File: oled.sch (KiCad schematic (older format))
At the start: 3 parts

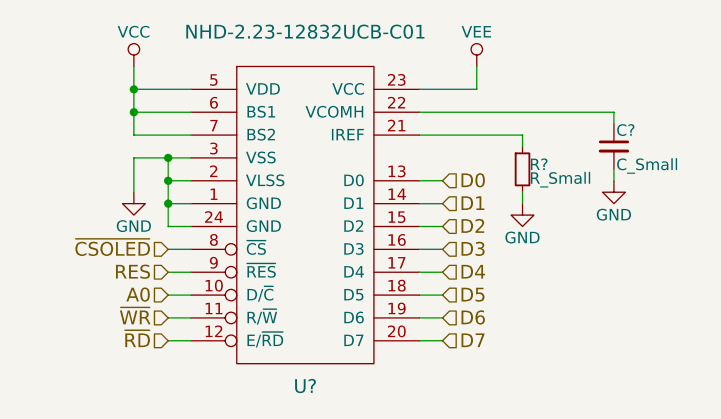
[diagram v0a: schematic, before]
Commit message: add more circuitry to schematic
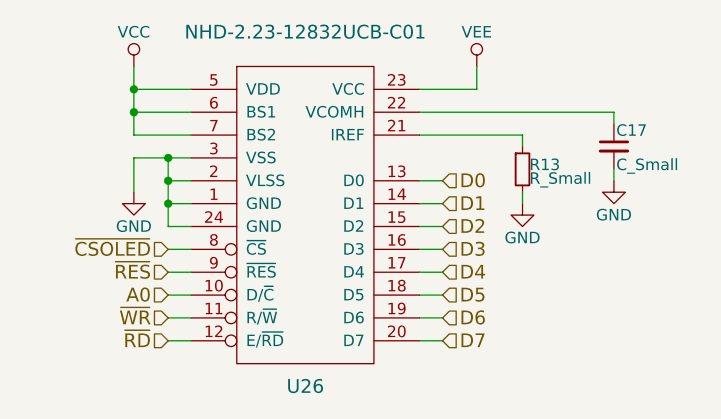
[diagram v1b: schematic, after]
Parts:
- gave numbers to parts that had none: 3
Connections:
- net RES renamed ~RES
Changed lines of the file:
@@
 $EndDescr
 $Comp
-L NHD-2.23-12832UCB-C01 U?
+L NHD-2.23-12832UCB-C01 U26
 U 1 1 576ACF58
 P 5500 3750
-F 0 "U?" H 5500 3000 60  0000 C CNN
+F 0 "U26" H 5500 3000 60  0000 C CNN
 F 1 "NHD-2.23-12832UCB-C01" H 5500 4550 60  0000 C CNN
 F 2 "" H 5500 3750 60  0000 C CNN
@@
 $EndComp
 $Comp
-L VCC #PWR?
+L VCC #PWR26
 U 1 1 576ACFE9
 P 4750 3100
-F 0 "#PWR?" H 4750 2950 50  0001 C CNN
+F 0 "#PWR26" H 4750 2950 50  0001 C CNN
 F 1 "VCC" H 4750 3250 50  0000 C CNN
 F 2 "" H 4750 3100 50  0000 C CNN
@@
 Connection ~ 4750 3300
 $Comp
-L GND #PWR?
+L GND #PWR29
 U 1 1 576AD010
 P 4750 3650
-F 0 "#PWR?" H 4750 3400 50  0001 C CNN
+F 0 "#PWR29" H 4750 3400 50  0001 C CNN
 F 1 "GND" H 4750 3500 50  0000 C CNN
 F 2 "" H 4750 3650 50  0000 C CNN
@@
 Text HLabel 4900 3900 0    60   Input ~ 0
 ~CSOLED
-Text HLabel 4900 4000 0    60   Input ~ 0
-RES
 Text HLabel 4900 4100 0    60   Input ~ 0
 A0
@@
 	6100 4300 6000 4300
 $Comp
-L VEE #PWR?
+L VEE #PWR27
 U 1 1 576CD337
 P 6250 3100
-F 0 "#PWR?" H 6250 2950 50  0001 C CNN
+F 0 "#PWR27" H 6250 2950 50  0001 C CNN
 F 1 "VEE" H 6250 3250 50  0000 C CNN
 F 2 "" H 6250 3100 50  0000 C CNN
@@
 	6250 3200 6250 3100
 $Comp
-L C_Small C?
+L C_Small C17
 U 1 1 576CD377
 P 6850 3450
-F 0 "C?" H 6860 3520 50  0000 L CNN
+F 0 "C17" H 6860 3520 50  0000 L CNN
 F 1 "C_Small" H 6860 3370 50  0000 L CNN
 F 2 "" H 6850 3450 50  0000 C CNN
@@
 	6850 3300 6850 3350
 $Comp
-L GND #PWR?
+L GND #PWR28
 U 1 1 576CD3C6
 P 6850 3600
-F 0 "#PWR?" H 6850 3350 50  0001 C CNN
+F 0 "#PWR28" H 6850 3350 50  0001 C CNN
 F 1 "GND" H 6850 3450 50  0000 C CNN
 F 2 "" H 6850 3600 50  0000 C CNN
@@
 	6850 3550 6850 3600
 $Comp
-L R_Small R?
+L R_Small R13
 U 1 1 576CD406
 P 6450 3550
-F 0 "R?" H 6480 3570 50  0000 L CNN
+F 0 "R13" H 6480 3570 50  0000 L CNN
 F 1 "R_Small" H 6480 3510 50  0000 L CNN
 F 2 "" H 6450 3550 50  0000 C CNN
@@
 	6450 3400 6450 3450
 $Comp
-L GND #PWR?
+L GND #PWR30
 U 1 1 576CD47B
 P 6450 3700
-F 0 "#PWR?" H 6450 3450 50  0001 C CNN
+F 0 "#PWR30" H 6450 3450 50  0001 C CNN
 F 1 "GND" H 6450 3550 50  0000 C CNN
 F 2 "" H 6450 3700 50  0000 C CNN
@@
 Wire Wire Line
 	6450 3650 6450 3700
+Text HLabel 4900 4000 0    60   Input ~ 0
+~RES
 $EndSCHEMATC
